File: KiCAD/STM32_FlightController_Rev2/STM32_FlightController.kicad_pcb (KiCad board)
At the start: 4 copper layers, 42 x 44.4 mm, 72 parts, among them J1 USB_B_Micro, J11 GPS_V_{IN}, J12 GPS_TX, J13 GND, J14 GPS_RX, J15 ELRS_V_{IN}, J16 GND, J17 ELRS_TX, J18 ELRS_RX, J19 Conn_02x05_Odd_Even, J2 GND, J3 BAT, J4 CRT, J5 5V, J6 S1, J7 S2, J8 S3, J9 S4, Q1 IRLML6244, Q2 IRLML6244, SW1 PTS815SJM, SW2 SW_SPDT, U1 USBLC6-2SC6, U2 AMS1117-3.3, U3 TLV70018, U4 STM32F405RGTx, U5 BMP390L, U6 ICM-20948, Y1 8MHz

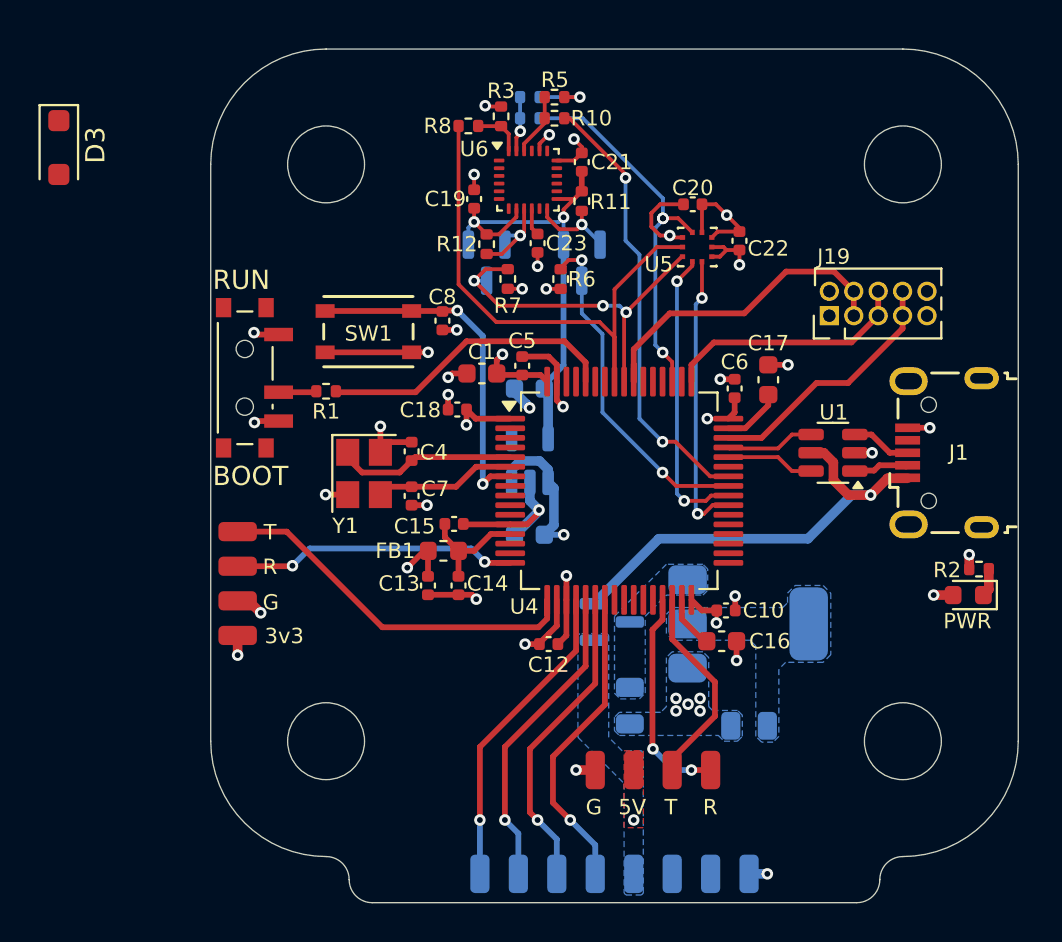
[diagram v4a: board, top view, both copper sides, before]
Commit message: re-speccing the power mux to PMEG2005CT,215 rated for 500 mA
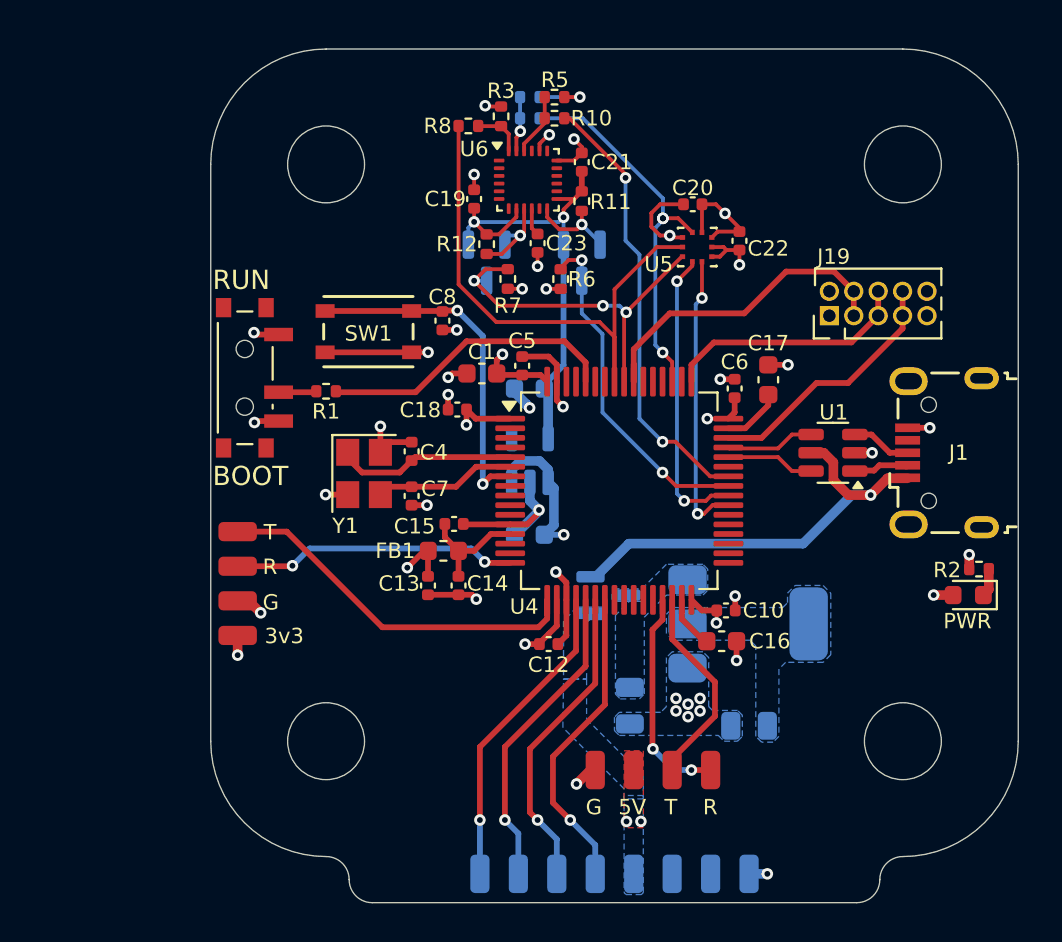
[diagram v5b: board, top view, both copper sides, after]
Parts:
- removed D3: PMEG6010CEH, Diode_SMD:D_SOD-123F
- D2: value BAT54C -> PMEG2005CT,215
- R10, R8, R9: value 3.3k -> 2.7k
- R3, R4, R5: value 2.7k -> 3.3k
- moved D2 1.41 mm to (114.4, 72.9)
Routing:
- net VBUS: track 23.6 -> 22.9 mm
- net GND: track 59.9 -> 60.2 mm, vias 36 -> 37
- net +5V: vias 1 -> 2

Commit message: replaced transistors with level shifter ICs
transistors appeared to switch to slowly for SPI, ICs seemed like they would be fast enough
required significant rerouting of SPI traces from sensors
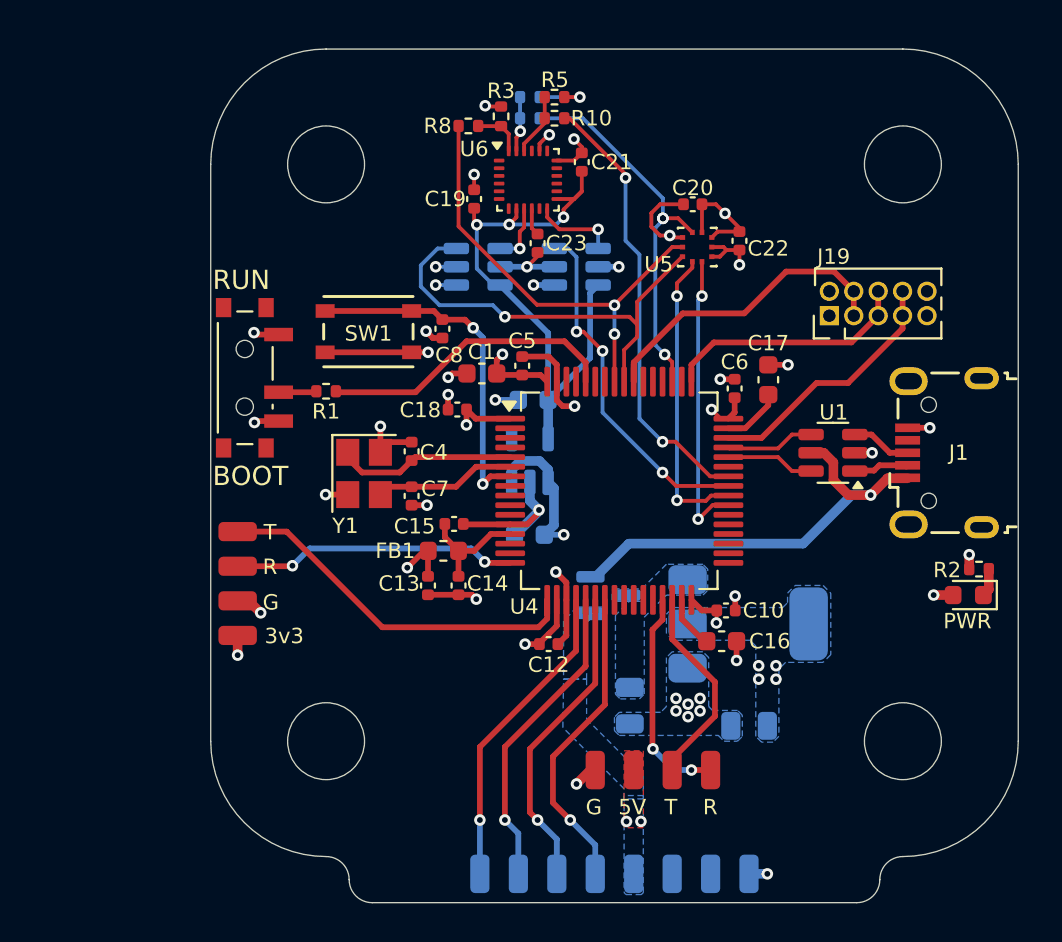
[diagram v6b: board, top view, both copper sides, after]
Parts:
- removed Q1, Q2: IRLML6244, Package_TO_SOT_SMD:SOT-23
- removed R11, R12, R6, R7: 4.7k, Resistor_SMD:R_0402_1005Metric
- added U7: SN74LVC1T45DBV, Package_TO_SOT_SMD:SOT-23-6, B.Cu at (112.8, 55.9)
- added U8: SN74LVC1T45DBV, Package_TO_SOT_SMD:SOT-23-6, B.Cu at (107.7, 55.9)
- moved C9 0.62 mm to (110.5, 62.8)
- moved C8 0.42 mm to (105.8, 59.1)
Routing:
- net GND: track 60.2 -> 66.1 mm, vias 37 -> 39
- net /MOSI: track 29.1 -> 23.8 mm, vias 0 -> 2
- net /MISO: track 19.1 -> 23.8 mm, vias 3 -> 1
- net +1V8: track 26.4 -> 30.6 mm, vias 2 -> 3
- net /IMU_MISO: track 4.79 -> 3.19 mm
- net /INT1: track 17.7 -> 18.3 mm, vias 2 -> 3
- net +3V3: track 37.0 -> 37.6 mm, vias 13 -> 17

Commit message: 90 ohm impedance matching for USB traces
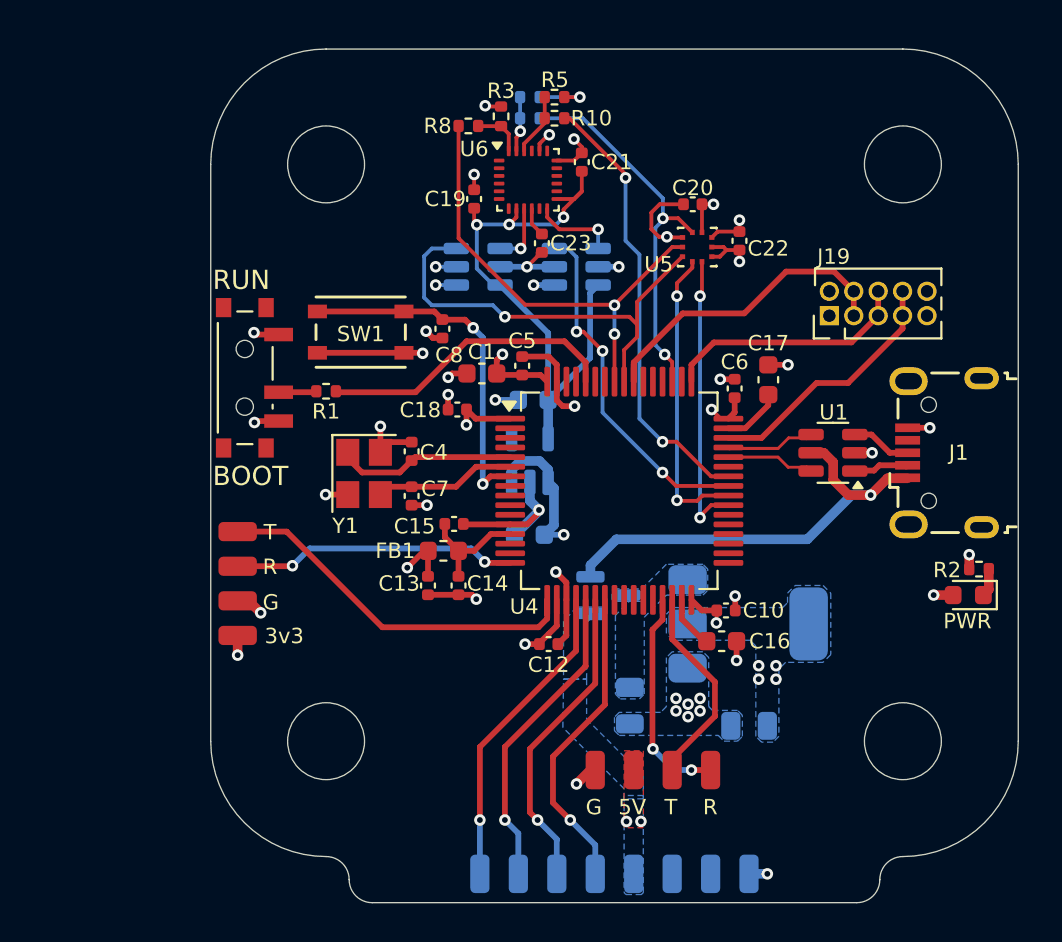
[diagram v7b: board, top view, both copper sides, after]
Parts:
- moved SW1 0.40 mm to (101.5, 59.2)
- moved C23 0.22 mm to (111.0, 54.6)
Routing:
- net +3V3: track 37.6 -> 36.1 mm, vias 17 -> 18
- net VBUS: track 22.9 -> 23.5 mm
- net /SCK: vias 3 -> 2

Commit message: replaced pads with corresponding JST-SH connectors
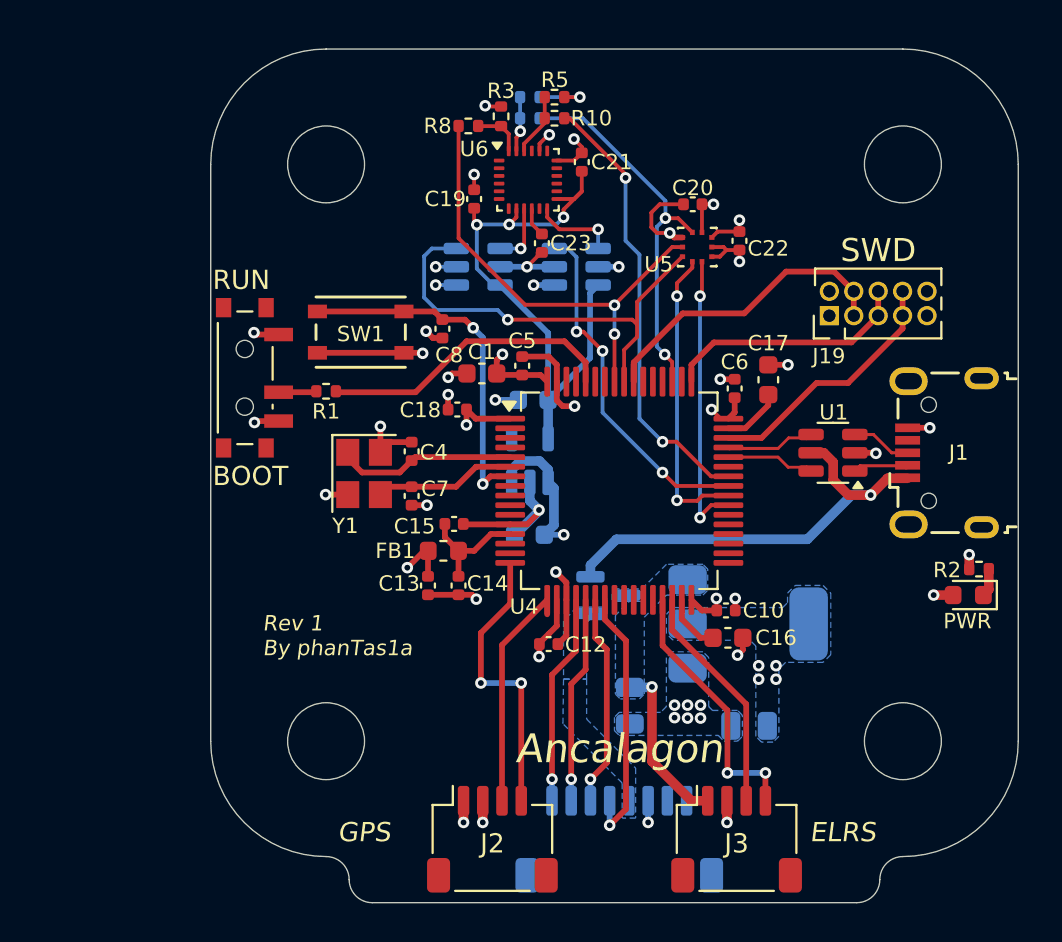
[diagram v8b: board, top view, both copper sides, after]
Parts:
- removed J11: GPS_V_{IN}, Connector_Wire:SolderWirePad_1x01_SMD_1x2mm
- removed J12: GPS_TX, Connector_Wire:SolderWirePad_1x01_SMD_1x2mm
- removed J13, J16: GND, Connector_Wire:SolderWirePad_1x01_SMD_1x2mm
- removed J14: GPS_RX, Connector_Wire:SolderWirePad_1x01_SMD_1x2mm
- removed J15: ELRS_V_{IN}, Connector_Wire:SolderWirePad_1x01_SMD_1x2mm
- removed J17: ELRS_TX, Connector_Wire:SolderWirePad_1x01_SMD_1x2mm
- removed J18: ELRS_RX, Connector_Wire:SolderWirePad_1x01_SMD_1x2mm
- removed J4: CRT, Connector_Wire:SolderWirePad_1x01_SMD_1x2mm
- removed J5: 5V, Connector_Wire:SolderWirePad_1x01_SMD_1x2mm
- removed J6: S1, Connector_Wire:SolderWirePad_1x01_SMD_1x2mm
- removed J7: S2, Connector_Wire:SolderWirePad_1x01_SMD_1x2mm
- removed J8: S3, Connector_Wire:SolderWirePad_1x01_SMD_1x2mm
- removed J9: S4, Connector_Wire:SolderWirePad_1x01_SMD_1x2mm
- added J10: Conn_01x08_Pin, Connector_JST:JST_SH_SM08B-SRSS-TB_1x08-1MP_P1.00mm_Horizontal, B.Cu at (115.0, 85.6)
- J2: value GND -> Conn_01x04_Pin; footprint Connector_Wire:SolderWirePad_1x01_SMD_1x2mm -> Connector_JST:JST_SH_SM04B-SRSS-TB_1x04-1MP_P1.00mm_Horizontal; moved to F.Cu
- J3: value BAT -> Conn_01x04_Pin; footprint Connector_Wire:SolderWirePad_1x01_SMD_1x2mm -> Connector_JST:JST_SH_SM04B-SRSS-TB_1x04-1MP_P1.00mm_Horizontal; moved to F.Cu
- moved J2 13.5 mm to (108.4, 85.6), turned to 0 degrees
- moved J3 2.25 mm to (121.1, 85.6), turned to 0 degrees
- moved C16 0.37 mm to (120.7, 75.2)
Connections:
- C2 pad 1: /V_MAIN -> V_MAIN
- D2 pad 3: /V_MAIN -> V_MAIN
- J2 pad 1: GND -> +3V3
- J3 pad 1: /BAT -> V_MAIN
- U2 pad 3: /V_MAIN -> V_MAIN
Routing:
- net V_MAIN: track 0.00 -> 8.78 mm, vias 0 -> 1
- net /GPS_TX: track 20.1 -> 12.2 mm
- net /S3: track 16.3 -> 10.8 mm
- net /S4: track 16.3 -> 11.0 mm
- net /S2: track 16.2 -> 11.1 mm
- net /S1: track 16.3 -> 13.8 mm
- net /ELRS_RX: track 11.4 -> 13.8 mm
- net /ELRS_TX: track 10.7 -> 12.0 mm
- net +5V: vias 2 -> 0
- added copper zone on B.Cu, net V_MAIN
- removed copper zone on F.Cu, net +5V
- removed copper zone on B.Cu, net /V_MAIN
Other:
- board text added: "Ancalagon"
- board text added: "ELRS"
- board text added: "ESC"
- board text added: "GPS"
- board text added: "Rev 1 By phanTas1a"
- board text added: "SWD"
- board text removed: "3v3"
- board text removed: "5V"
- board text removed: "B"
- board text removed: "C"
- board text removed: "G"
- board text removed: "R"
- board text removed: "S1"
- board text removed: "S2"
- board text removed: "S3"
- board text removed: "S4"
- board text removed: "T"
